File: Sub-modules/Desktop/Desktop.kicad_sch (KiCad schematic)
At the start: 57 parts, among them J1 USB_C_Receptacle_USB2.0_14P, J2 PR5L5015-5P-C-H, J3 PR5L5015-5P-C-H, SW1 SKRPACE010, SW2 SW_Push, SW3 SKRPACE010, U1 W25Q16JVSS, U10 AT24CS02-SSHM, U2 MAX40200AUK, U3 RP2040, U4 TLV75733PDBV, U5 SHT4x, U6 STHS34PF80, U7 VEML7700-TT, U8 MCP79410, Y1 ABM8-272-T3, Y2 X1A0000610006

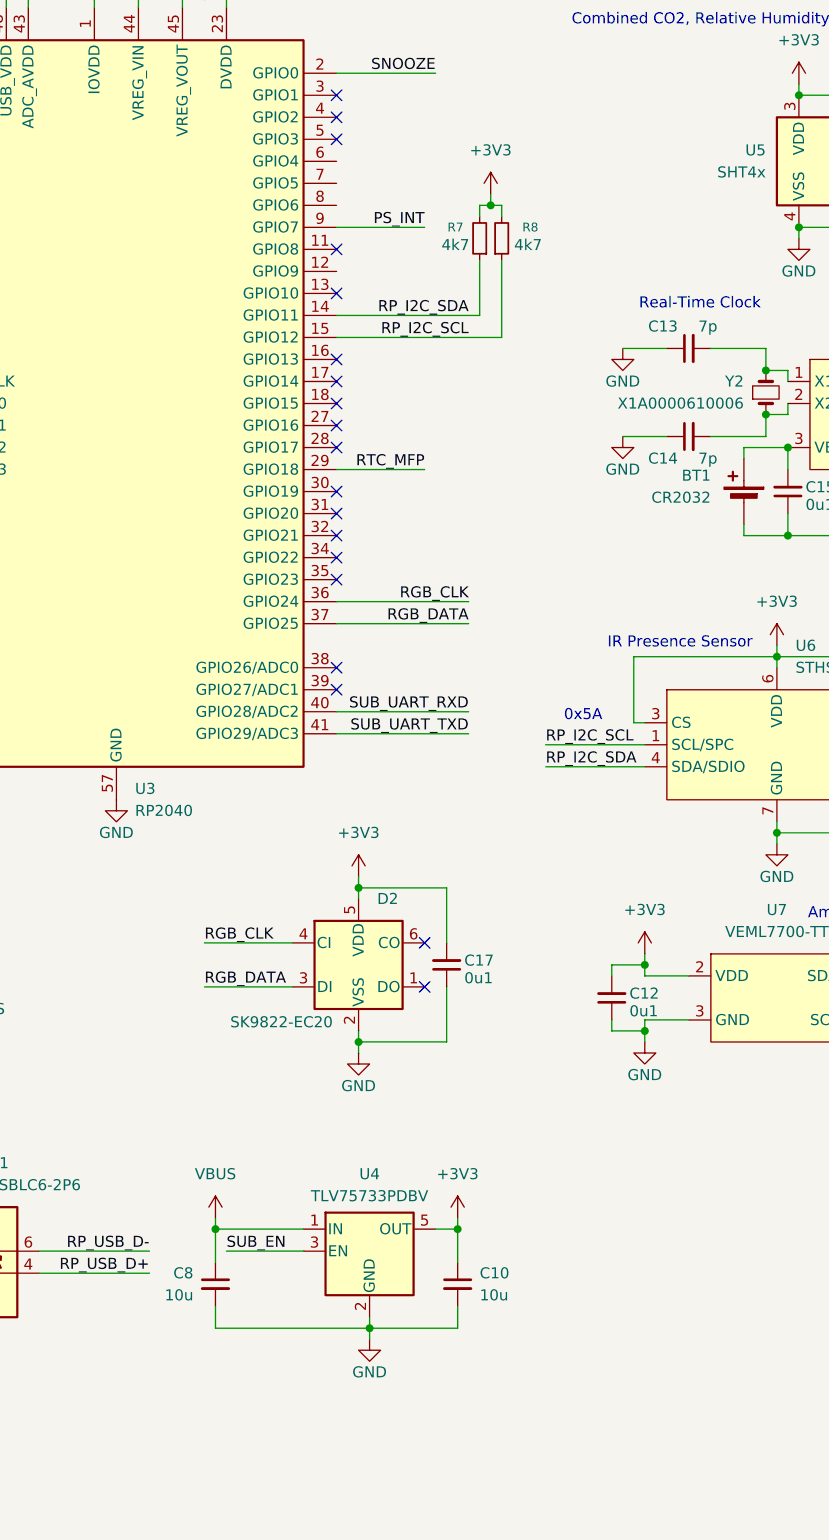
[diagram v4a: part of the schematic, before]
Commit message: Desktop v1.15: Changed I2C pins to 10 and 11 to fix I2C incompatibility issue, changed RGB LED to Neopixel
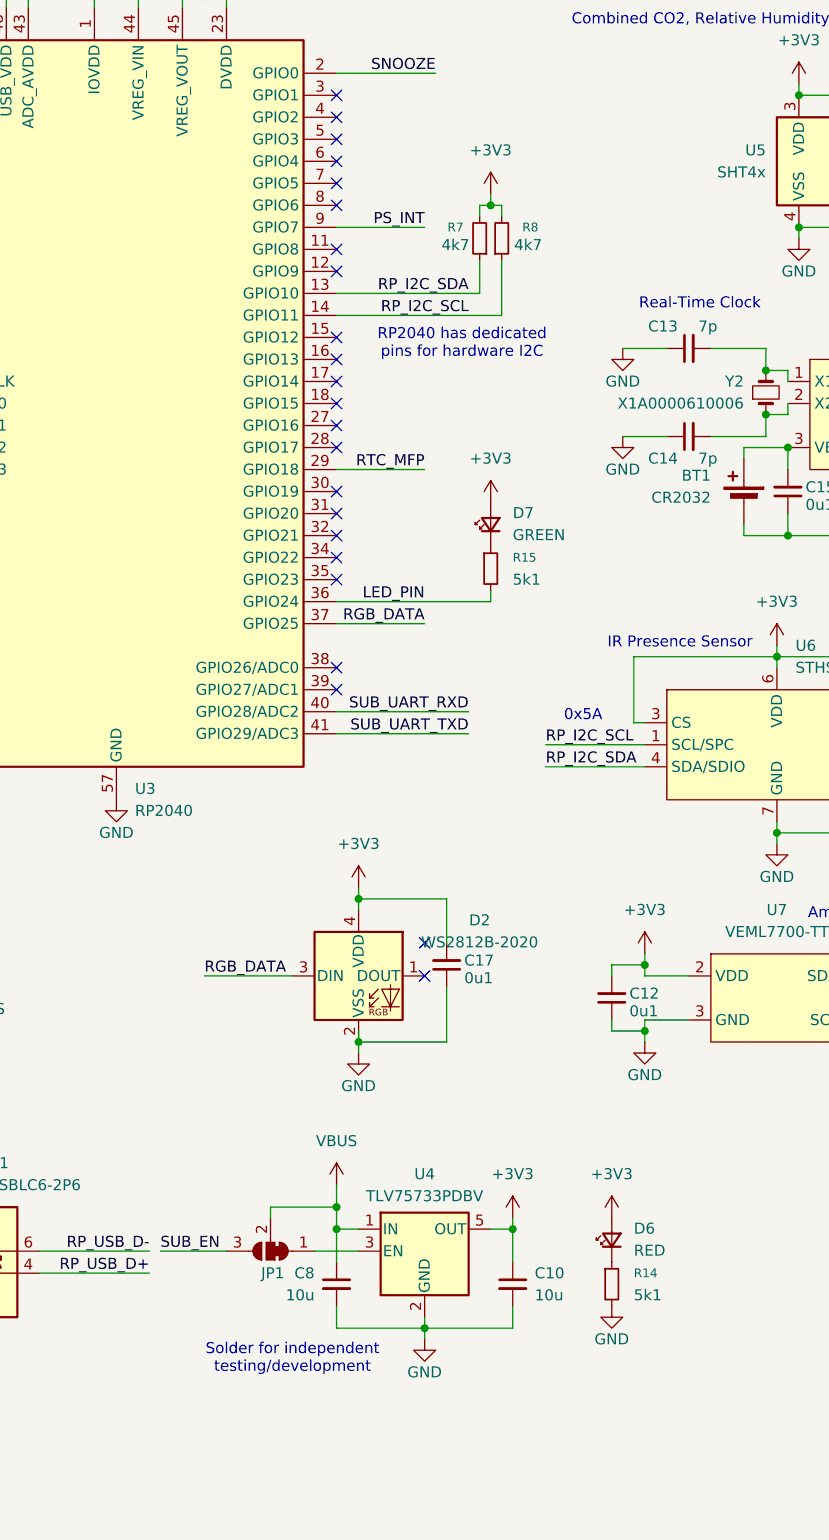
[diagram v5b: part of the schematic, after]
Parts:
- removed D2: SK9822-EC20, PCM_SparkFun-LED:APA102_2020-6Pin, symbol PCM_SparkFun-LED:APA102_2020-6Pin
- added D2: WS2812B-2020, LED_SMD:LED_WS2812B-2020_PLCC4_2.0x2.0mm, symbol LED:WS2812B-2020
- added D6: RED, LED_SMD:LED_0805_2012Metric, symbol Device:LED_Small
- added D7: GREEN, LED_SMD:LED_0805_2012Metric, symbol Device:LED_Small
- added JP1: SolderJumper_3_Bridged12, Jumper:SolderJumper-3_P1.3mm_Bridged12_RoundedPad1.0x1.5mm, symbol Jumper:SolderJumper_3_Bridged12
- added R14, R15: 5k1, PCM_Resistor_SMD_AKL:R_0402_1005Metric, symbol Device:R_Small
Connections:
- net +3V3: now also D2.4 (VDD), D6.2 (A), D7.2 (A)
- net GND: now also D2.2 (VSS), R14.2
- net RGB_DATA: now also D2.3 (DIN)
- net RP_I2C_SCL: now also U3.14 (GPIO11); no longer U3.15 (GPIO12)
- net RP_I2C_SDA: now also U3.13 (GPIO10); no longer U3.14 (GPIO11)
- net SUB_EN: now also JP1.3 (B); no longer U4.3 (EN)
- net VBUS: now also JP1.2 (C)
- net RGB_CLK renamed LED_PIN
- net LED_PIN: now also R15.2
- new net: JP1.1 (A), U4.3 (EN)
- new net: D7.1 (K), R15.1
- new net: D6.1 (K), R14.1
- no-connect marks 23 -> 27
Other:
- note added: "RP2040 has dedicated pins for hardware I2C"
- note added: "Solder for independent testing/development"
- title: (none) -> Desktop
- moved on the sheet: C10, C8, U4
